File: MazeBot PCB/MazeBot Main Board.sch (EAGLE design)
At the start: 33 parts, among them IC1 7805TV, IC2 L298

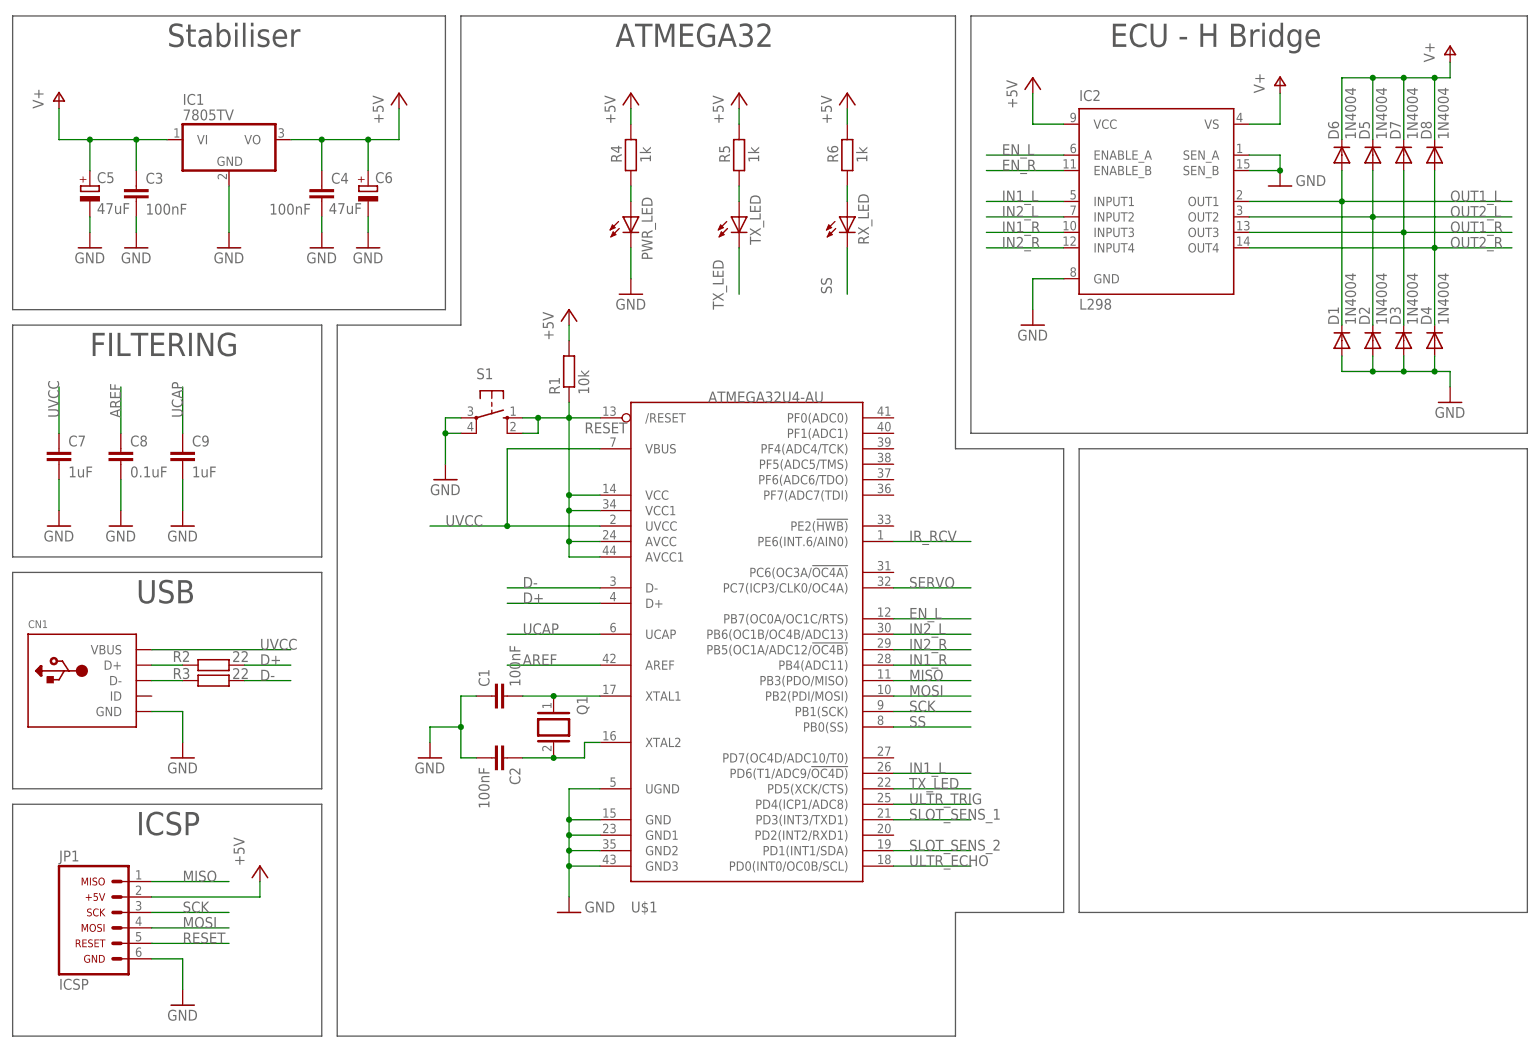
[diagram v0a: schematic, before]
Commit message: Add IR remote
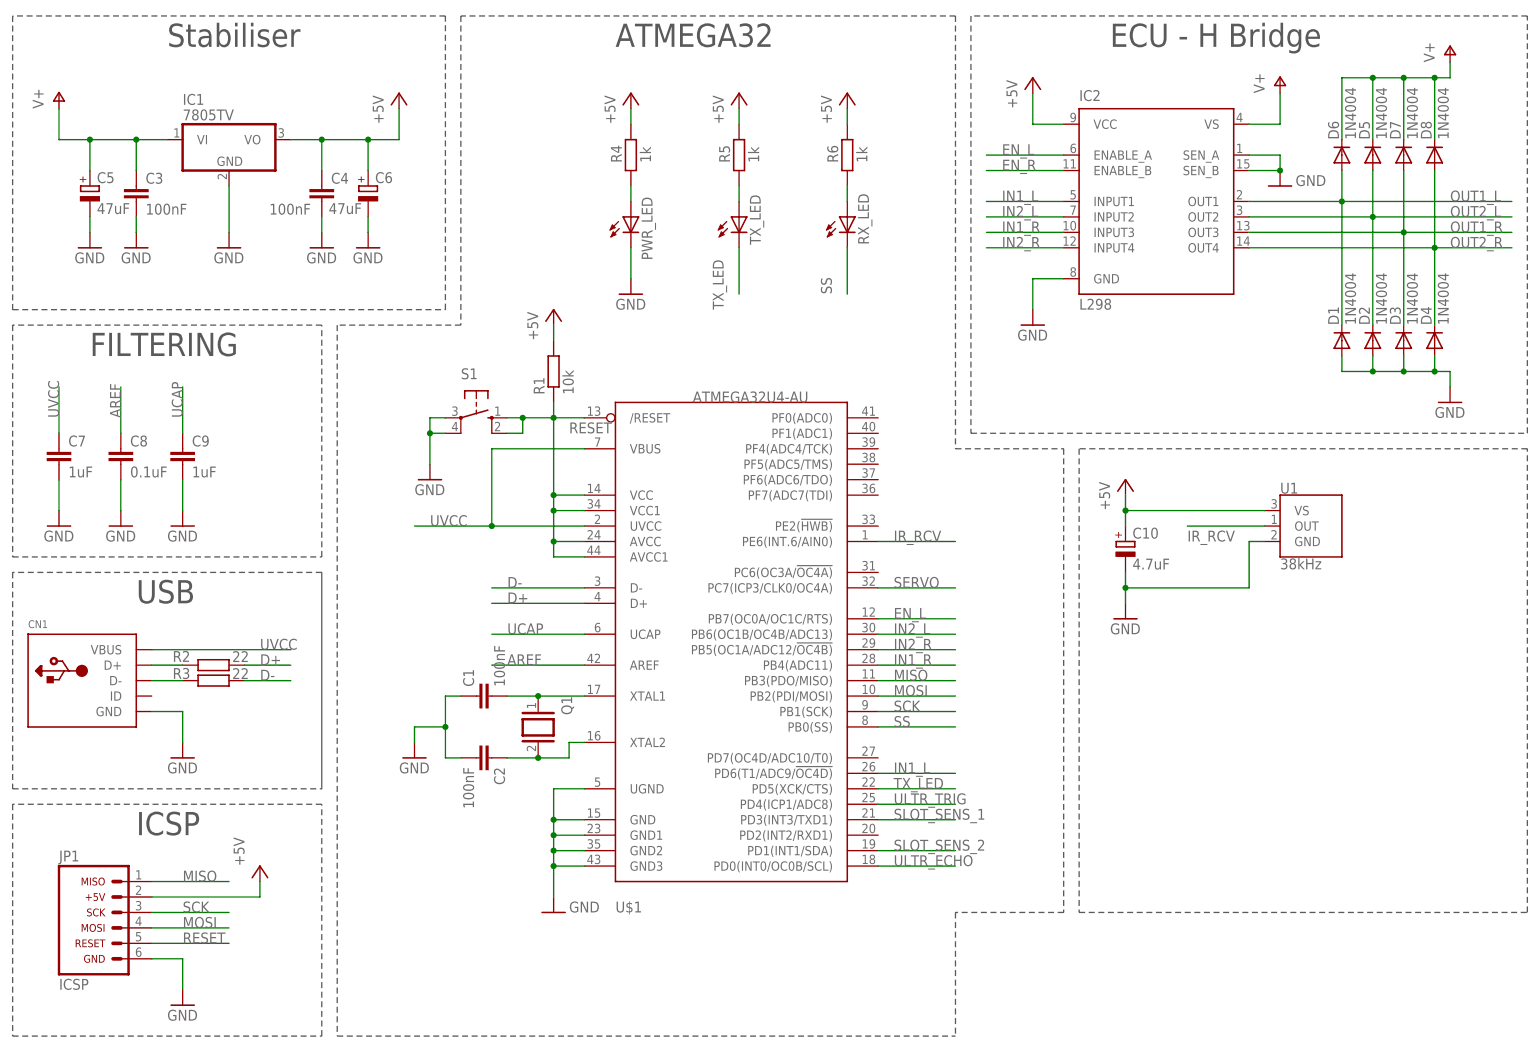
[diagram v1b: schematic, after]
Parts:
- added C10: 4.7uF, rcl:CPOL-EUE2-5
- added U1: 38kHz, SparkFun-Sensors:TSOP38238
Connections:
- net +5V: now also C10.+, U1.VS
- net GND: now also C10.-, U1.GND
- net IR_RCV: now also U1.OUT
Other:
- moved on the sheet: C1, C2, Q1, R1, S1, U$1

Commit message: Add IO Ports
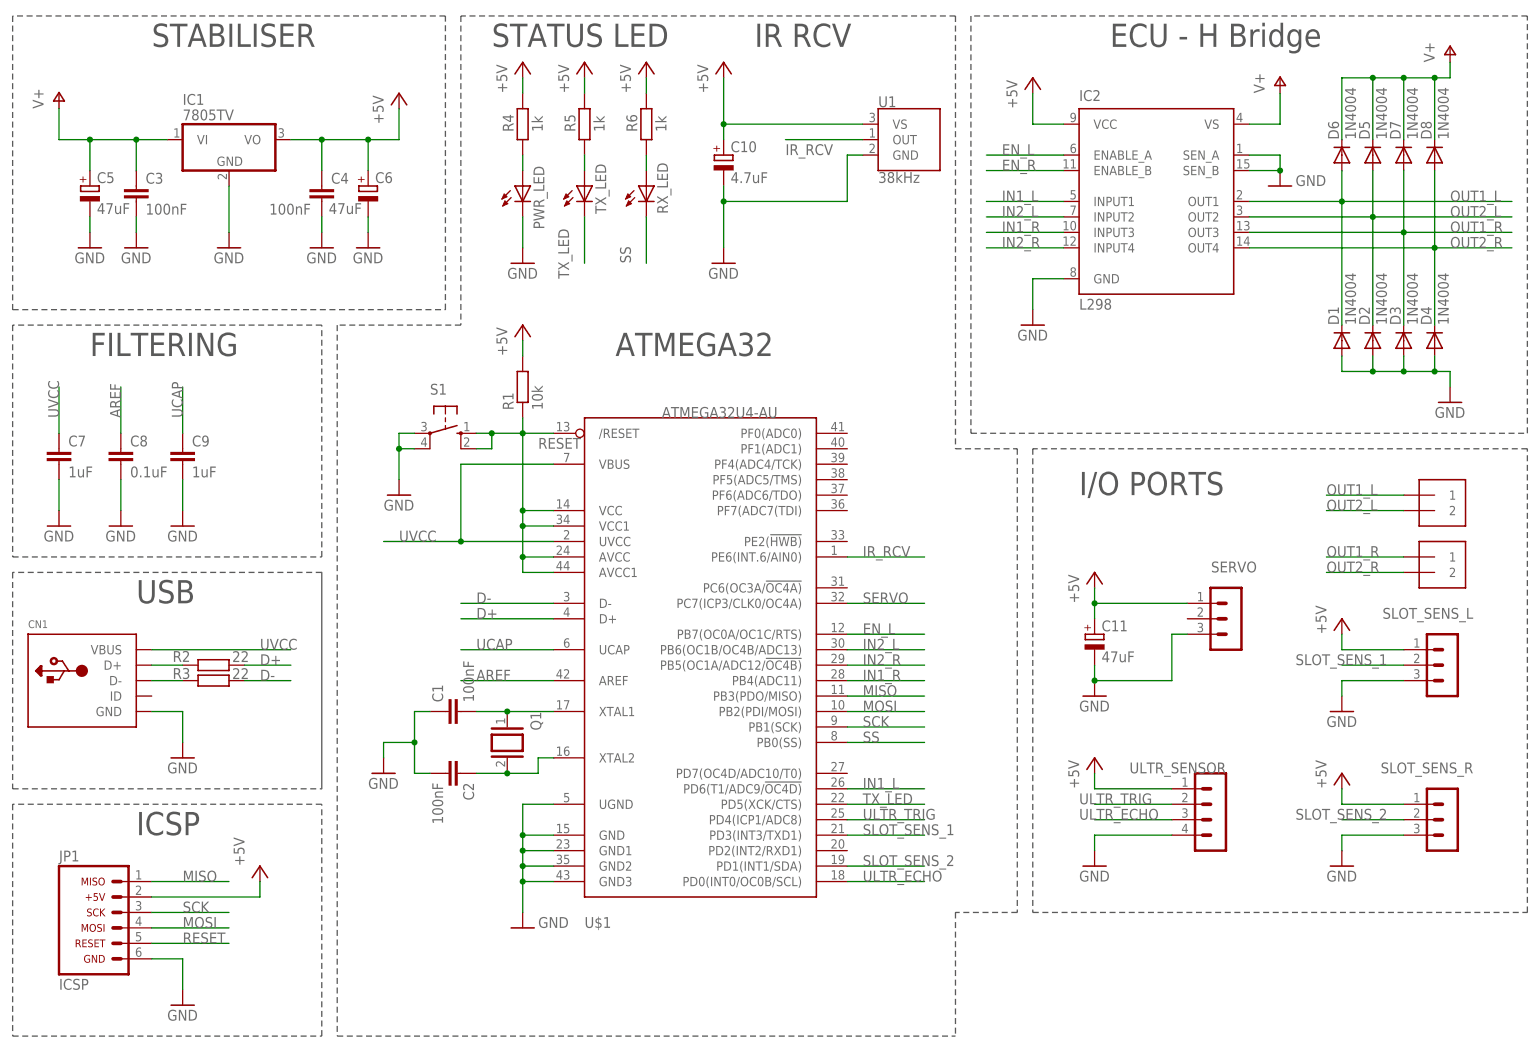
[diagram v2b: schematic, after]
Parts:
- added C11: 47uF, rcl:CPOL-EUE2-5
- added MOT_L, MOT_R: 1X2-3.5MM, adafruit:1X2-3.5MM
- added SERVO, SLOT_SENS_L, SLOT_SENS_R: (no value), con-lstb:MA03-1
- added ULTR_SENSOR: (no value), con-lstb:MA04-1
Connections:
- net +5V: now also C11.+, SERVO.1, SLOT_SENS_L.1, SLOT_SENS_R.1, ULTR_SENSOR.1
- net GND: now also C11.-, SERVO.3, SLOT_SENS_L.3, SLOT_SENS_R.3, ULTR_SENSOR.4
- net OUT1_L: now also MOT_L.1
- net OUT1_R: now also MOT_R.1
- net OUT2_L: now also MOT_L.2
- net OUT2_R: now also MOT_R.2
- net SLOT_SENS_1: now also SLOT_SENS_L.2
- net SLOT_SENS_2: now also SLOT_SENS_R.2
- net ULTR_ECHO: now also ULTR_SENSOR.3
- net ULTR_TRIG: now also ULTR_SENSOR.2
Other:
- note added: "I/O PORTS"
- note added: "IR RCV"
- note added: "STABILISER"
- note added: "STATUS LED"
- note removed: "Stabiliser"
- moved on the sheet: C1, C10, C2, PWR_LED, Q1, R1, R4, R5, R6, RX_LED, S1, TX_LED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

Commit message: Fix major ERC issues
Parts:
- Q1: value (none) -> 16MHz
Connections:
- net EN_R: now also U$1.PC6(OC3A/!OC4A)
- net SERVO: now also SERVO.2
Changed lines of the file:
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@@
 <layer number="91" name="Nets" color="2" fill="1" visible="yes" active="yes"/>
 <layer number="92" name="Busses" color="1" fill="1" visible="yes" active="yes"/>
-<layer number="93" name="Pins" color="2" fill="1" visible="no" active="yes"/>
+<layer number="93" name="Pins" color="2" fill="1" visible="yes" active="yes"/>
 <layer number="94" name="Symbols" color="4" fill="1" visible="yes" active="yes"/>
 <layer number="95" name="Names" color="7" fill="1" visible="yes" active="yes"/>
@@
 <part name="GND8" library="supply1" library_urn="urn:adsk.eagle:library:371" deviceset="GND" device=""/>
 <part name="P+5" library="supply1" library_urn="urn:adsk.eagle:library:371" deviceset="V+" device=""/>
-<part name="Q1" library="special" library_urn="urn:adsk.eagle:library:367" deviceset="XTAL/S" device="" package3d_urn="urn:adsk.eagle:package:26647/2"/>
+<part name="Q1" library="special" library_urn="urn:adsk.eagle:library:367" deviceset="XTAL/S" device="" package3d_urn="urn:adsk.eagle:package:26647/2" value="16MHz"/>
 <part name="U$1" library="adafruit" deviceset="ATMEGA32U4" device="-AU"/>
 <part name="C1" library="rcl" library_urn="urn:adsk.eagle:library:334" deviceset="C-EU" device="025-024X044" package3d_urn="urn:adsk.eagle:package:23630/1" value="100nF"/>
@@
 <part name="R2" library="rcl" library_urn="urn:adsk.eagle:library:334" deviceset="R-EU_" device="0207/10" package3d_urn="urn:adsk.eagle:package:23491/2" value="22"/>
 <part name="R3" library="rcl" library_urn="urn:adsk.eagle:library:334" deviceset="R-EU_" device="0207/10" package3d_urn="urn:adsk.eagle:package:23491/2" value="22"/>
-<part name="FRAME1" library="frames" library_urn="urn:adsk.eagle:library:229" deviceset="A4L-LOC" device=""/>
+<part name="FRAME1" library="frames" library_urn="urn:adsk.eagle:library:229" deviceset="A4L-LOC" device="" value="Maciej Ziaja"/>
 <part name="P+8" library="supply1" library_urn="urn:adsk.eagle:library:371" deviceset="+5V" device=""/>
 <part name="R4" library="rcl" library_urn="urn:adsk.eagle:library:334" deviceset="R-EU_" device="0207/10" package3d_urn="urn:adsk.eagle:package:23491/2" value="1k"/>
@@
 </instance>
 <instance part="C11" gate="G$1" x="182.88" y="71.12" smashed="yes">
-<attribute name="NAME" x="184.023" y="71.6026" size="1.778" layer="95"/>
-<attribute name="VALUE" x="184.023" y="66.5226" size="1.778" layer="96"/>
+<attribute name="NAME" x="176.403" y="71.6026" size="1.778" layer="95"/>
+<attribute name="VALUE" x="176.403" y="66.5226" size="1.778" layer="96"/>
 </instance>
 <instance part="P+15" gate="1" x="182.88" y="81.28" smashed="yes">
@@
 <wire x1="177.8" y1="147.32" x2="165.1" y2="147.32" width="0.1524" layer="91"/>
 <label x="167.64" y="147.32" size="1.778" layer="95"/>
+</segment>
+<segment>
+<pinref part="U$1" gate="G$1" pin="PC6(OC3A/!OC4A)"/>
+<wire x1="142.24" y1="78.74" x2="154.94" y2="78.74" width="0.1524" layer="91"/>
+<label x="144.78" y="78.74" size="1.778" layer="95"/>
 </segment>
 </net>
@@
 <label x="144.78" y="76.2" size="1.778" layer="95"/>
 </segment>
-</net>
+<segment>
+<pinref part="SERVO" gate="G$1" pin="2"/>
+<wire x1="198.12" y1="73.66" x2="187.96" y2="73.66" width="0.1524" layer="91"/>
+<label x="187.96" y="73.66" size="1.778" layer="95"/>
+</segment>
+</net>

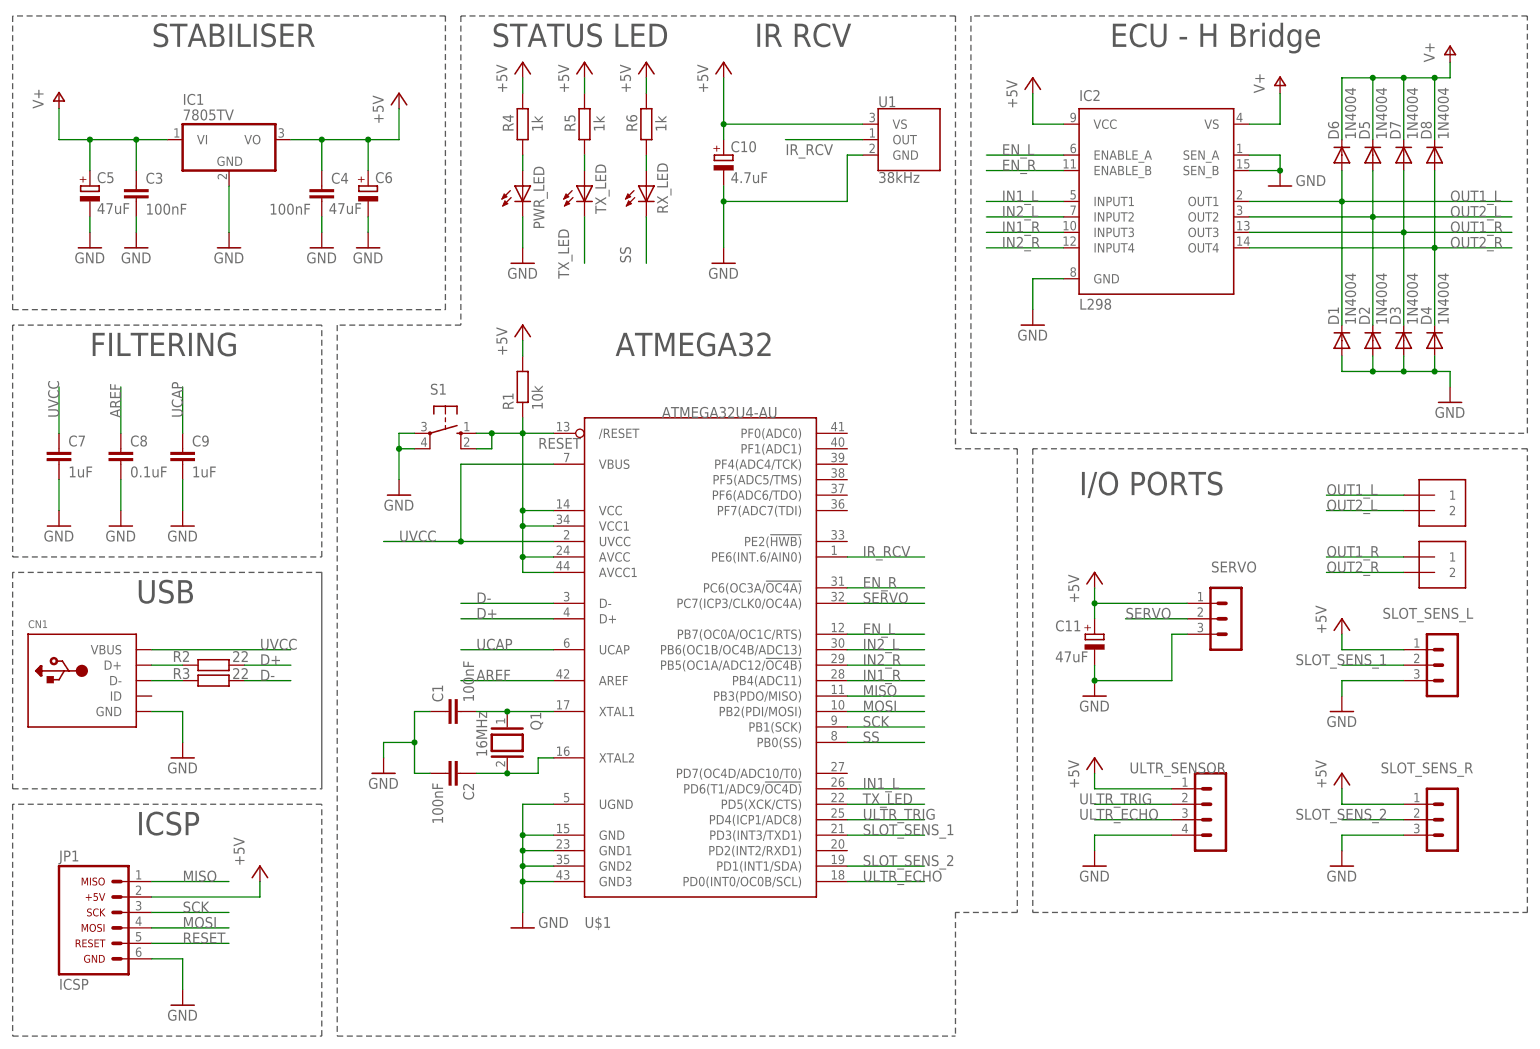
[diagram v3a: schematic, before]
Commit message: Add power in terminal
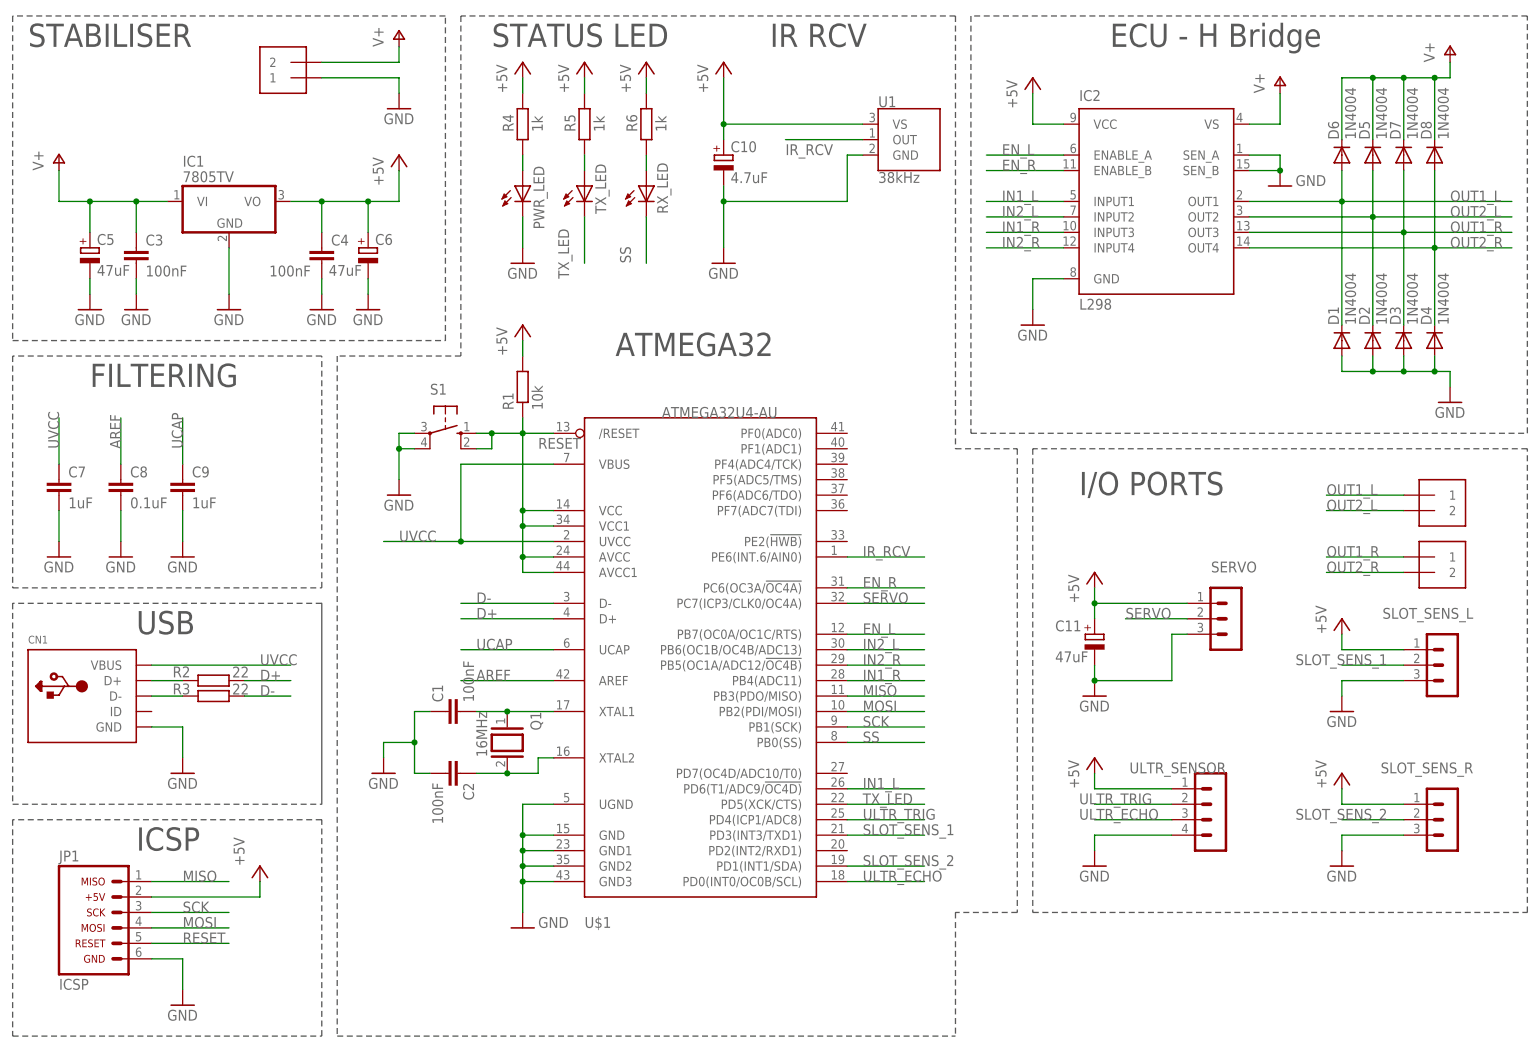
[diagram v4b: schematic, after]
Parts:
- added PWR_IN: 1X2-3.5MM, adafruit:1X2-3.5MM
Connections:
- net GND: now also PWR_IN.1
- net V+: now also PWR_IN.2
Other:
- moved on the sheet: C3, C4, C5, C6, C7, C8, C9, CN1, IC1, R2, R3

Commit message: Change to SMD and minor fixes
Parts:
- C10, C11, C5, C6: device rcl:CPOL-EUE2-5 -> rcl:CPOL-EUUD-6,3X8,8
- D1, D2, D3, D4, D5, D6, D7, D8: value 1N4004 -> GF1; device diode:1N4004 -> diode:GF1
- R1, R2, R3, R4, R5, R6: device rcl:R-EU_0207/10 -> eagle-ltspice:RR1206
- renumbered CN1 to USB, JP1 to ICSP, S1 to SW_RESET, U1 to IR_RCV
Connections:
- net OUT1_L renamed MOT1_L
- net OUT1_R renamed MOT1_R
- net OUT2_L renamed MOT2_L
- net OUT2_R renamed MOT2_R
